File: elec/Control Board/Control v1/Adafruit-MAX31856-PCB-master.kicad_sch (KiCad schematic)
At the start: 8 parts, among them J10 MCP9600, J8 MCP9600, J9 MCP9600_

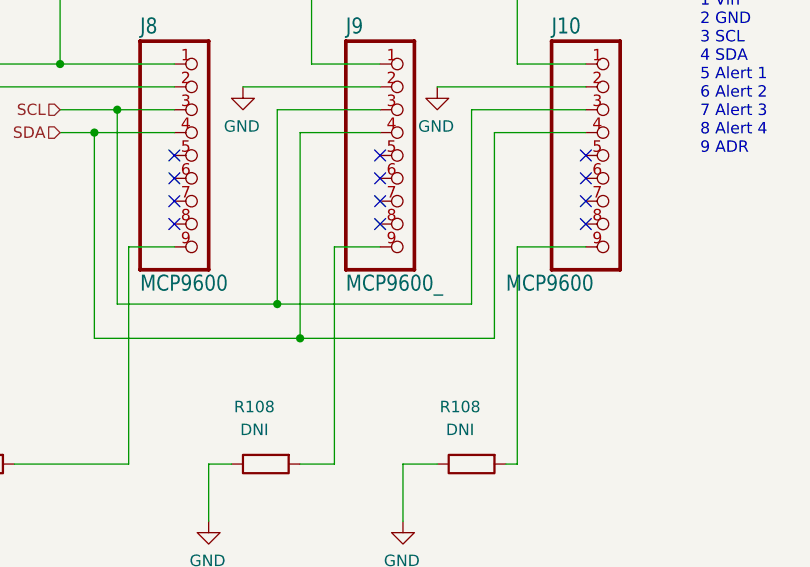
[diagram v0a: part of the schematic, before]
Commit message: Update parts in schematic for BOM generation.
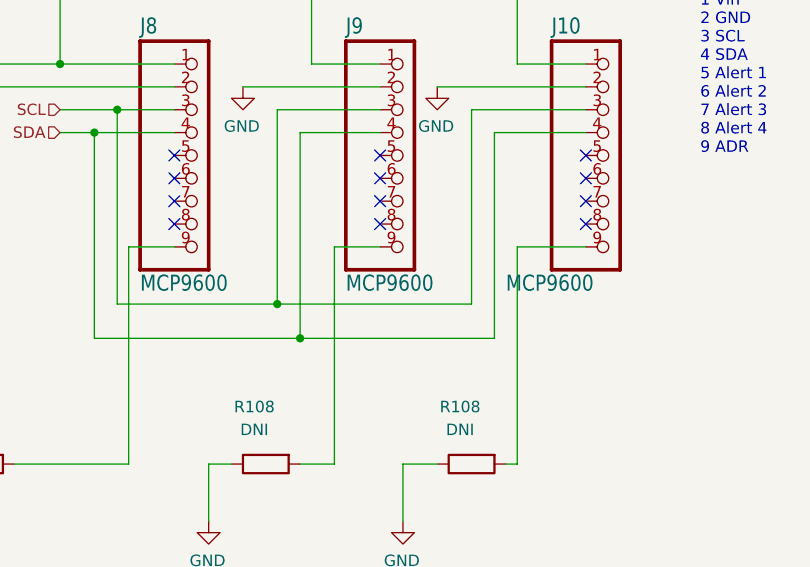
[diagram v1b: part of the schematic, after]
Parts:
- J10, J8: AssemblyType (none) -> HAND; Cost (none) -> 15.95; Distributor 1 (none) -> adafruit; Distributor 1 PN (none) -> 4101; MPN (none) -> 4101; Manufacturer (none) -> Adafruit
- J9: value MCP9600_ -> MCP9600; AssemblyType (none) -> HAND; Cost (none) -> 15.95; Distributor 1 (none) -> adafruit; Distributor 1 PN (none) -> 4101; MPN (none) -> 4101; Manufacturer (none) -> Adafruit
- TP103: Cost (none) -> NA
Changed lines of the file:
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@@
+      (effects (font (size 1.27 1.27)) hide)
+    )
+    (property "Cost" "NA" (at 88.9 34.29 0)
       (effects (font (size 1.27 1.27)) hide)
     )
@@
       (effects (font (size 1.27 1.27)) hide)
     )
-    (property "Datasheet" "" (at 149.86 53.34 0)
+    (property "Datasheet" "https://www.adafruit.com/product/4101" (at 149.86 53.34 0)
+      (effects (font (size 1.27 1.27)) hide)
+    )
+    (property "AssemblyType" "HAND" (at 149.86 53.34 0)
+      (effects (font (size 1.27 1.27)) hide)
+    )
+    (property "Cost" "15.95" (at 149.86 53.34 0)
+      (effects (font (size 1.27 1.27)) hide)
+    )
+    (property "Description" "Adafruit MCP9600 I2C Thermocouple Amplifier - K, J, T, N, S, E, B and R Type T" (at 149.86 53.34 0)
+      (effects (font (size 1.27 1.27)) hide)
+    )
+    (property "Distributor 1" "adafruit" (at 149.86 53.34 0)
+      (effects (font (size 1.27 1.27)) hide)
+    )
+    (property "Distributor 1 PN" "4101" (at 149.86 53.34 0)
+      (effects (font (size 1.27 1.27)) hide)
+    )
+    (property "MPN" "4101" (at 149.86 53.34 0)
+      (effects (font (size 1.27 1.27)) hide)
+    )
+    (property "Manufacturer" "Adafruit" (at 149.86 53.34 0)
       (effects (font (size 1.27 1.27)) hide)
     )
@@
       (effects (font (size 1.778 1.5113)) (justify left bottom))
     )
-    (property "Value" "MCP9600_" (at 120.65 68.58 0)
+    (property "Value" "MCP9600" (at 120.65 68.58 0)
       (effects (font (size 1.778 1.5113)) (justify left bottom))
     )
@@
       (effects (font (size 1.27 1.27)) hide)
     )
-    (property "Datasheet" "" (at 127 53.34 0)
+    (property "Datasheet" "https://www.adafruit.com/product/4101" (at 127 53.34 0)
+      (effects (font (size 1.27 1.27)) hide)
+    )
+    (property "AssemblyType" "HAND" (at 127 53.34 0)
+      (effects (font (size 1.27 1.27)) hide)
+    )
+    (property "Cost" "15.95" (at 127 53.34 0)
+      (effects (font (size 1.27 1.27)) hide)
+    )
+    (property "Description" "Adafruit MCP9600 I2C Thermocouple Amplifier - K, J, T, N, S, E, B and R Type T" (at 127 53.34 0)
+      (effects (font (size 1.27 1.27)) hide)
+    )
+    (property "Distributor 1" "adafruit" (at 127 53.34 0)
+      (effects (font (size 1.27 1.27)) hide)
+    )
+    (property "Distributor 1 PN" "4101" (at 127 53.34 0)
+      (effects (font (size 1.27 1.27)) hide)
+    )
+    (property "MPN" "4101" (at 127 53.34 0)
+      (effects (font (size 1.27 1.27)) hide)
+    )
+    (property "Manufacturer" "Adafruit" (at 127 53.34 0)
       (effects (font (size 1.27 1.27)) hide)
     )
@@
       (effects (font (size 1.27 1.27)) hide)
     )
-    (property "Datasheet" "" (at 104.14 53.34 0)
-      (effects (font (size 1.27 1.27)) hide)
-    )
+    (property "Datasheet" "https://www.adafruit.com/product/4101" (at 104.14 53.34 0)
+      (effects (font (size 1.27 1.27)) hide)
+    )
+    (property "AssemblyType" "HAND" (at 104.14 53.34 0)
+      (effects (font (size 1.27 1.27)) hide)
+    )
+    (property "Cost" "15.95" (at 104.14 53.34 0)
+      (effects (font (size 1.27 1.27)) hide)
+    )
+    (property "Description" "Adafruit MCP9600 I2C Thermocouple Amplifier - K, J, T, N, S, E, B and R Type T" (at 104.14 53.34 0)
+      (effects (font (size 1.27 1.27)) hide)
+    )
+    (property "Distributor 1" "adafruit" (at 104.14 53.34 0)
+      (effects (font (size 1.27 1.27)) hide)
+    )
+    (property "Distributor 1 PN" "4101" (at 104.14 53.34 0)
+      (effects (font (size 1.27 1.27)) hide)
+    )
+    (property "MPN" "4101" (at 104.14 53.34 0)
+      (effects (font (size 1.27 1.27)) hide)
+    )
+    (property "Manufacturer" "Adafruit" (at 104.14 53.34 0)
+      (effects (font (size 1.27 1.27)) hide)
+    )
